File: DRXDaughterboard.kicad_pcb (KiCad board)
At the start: 8 copper layers, 150.9 x 55.8 mm, 12 parts, among them J1 Samtec_ASP-134488-01, J2 Samtec_ASP-134488-01, J3 Conn_02x12_Odd_Even, J4 Samtec_ASP-134488-01, J5 Samtec_ASP-134488-01, J6 Conn_02x06_Odd_Even, J7 Samtec_ASP-134486-01, J8 Samtec_ASP-134486-01, U1 SN74LVC2T45DCUR

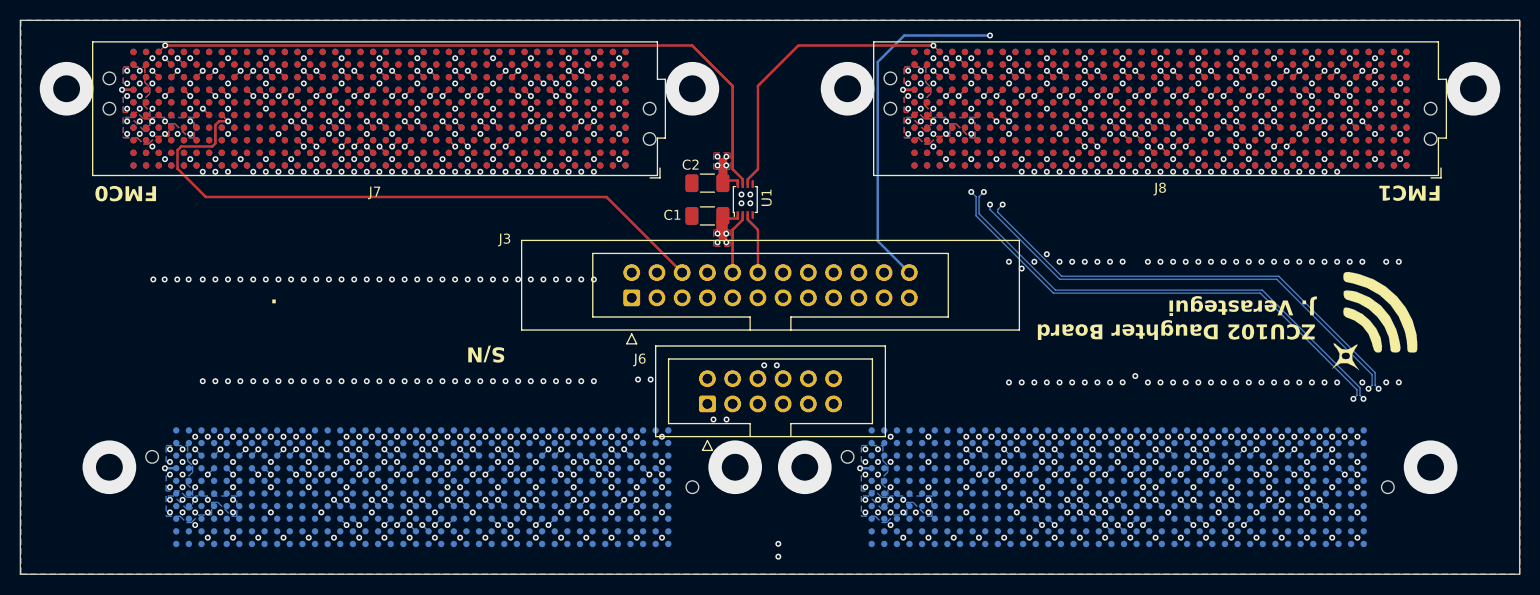
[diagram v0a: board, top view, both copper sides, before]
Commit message: Work on swapping fclk and lclk pins on J1/J4.  Add a power LED running powered by the +3.3V.  Rename.
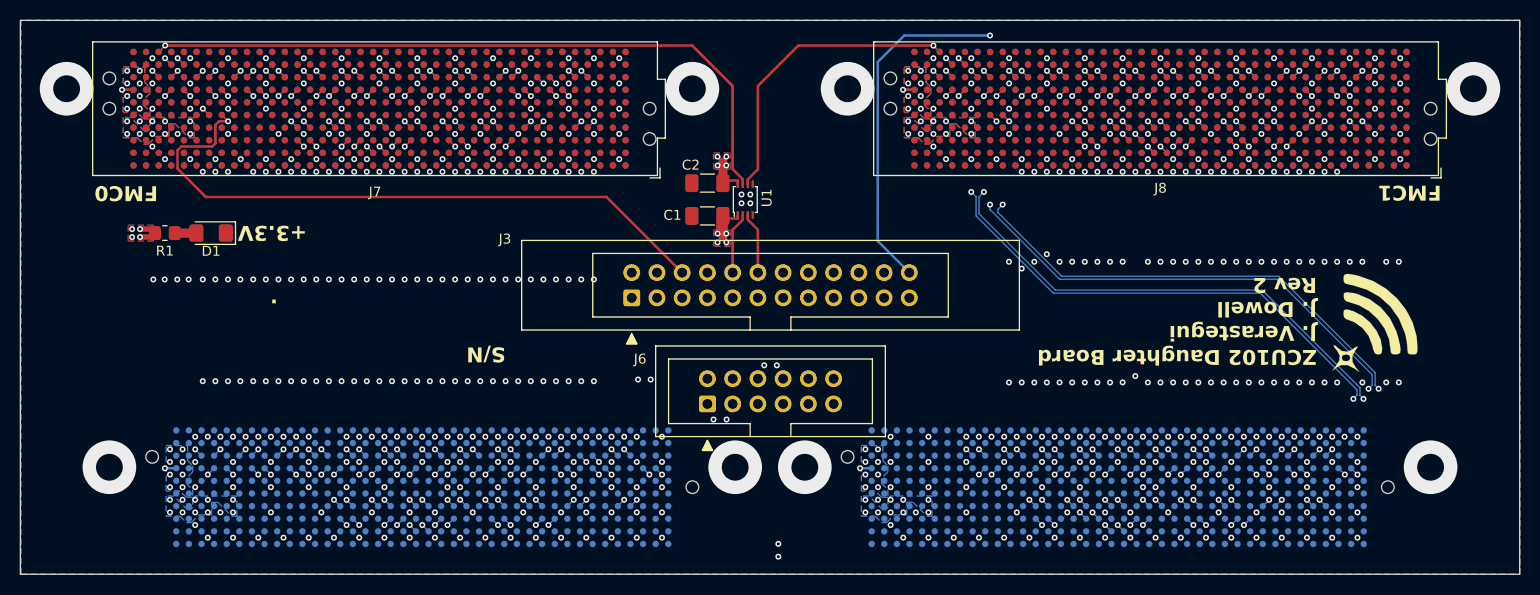
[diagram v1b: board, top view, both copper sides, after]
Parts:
- added D1: LED, LED_SMD:LED_1206_3216Metric_Pad1.42x1.75mm_HandSolder, F.Cu at (86.0, 91.6)
- added R1: 324, Resistor_SMD:R_0805_2012Metric_Pad1.20x1.40mm_HandSolder, F.Cu at (81.3, 91.6)
- moved G*** 0.19 mm to (203.7, 100.1)
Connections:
- J1 pad D4: FMC0_FCLKA_P -> FMC0_LCLKA_P
- J1 pad D5: FMC0_FCLKA_N -> FMC0_LCLKA_N
- J1 pad G2: FMC1_LCLKA_P -> FMC1_FCLKA_P
- J1 pad G3: FMC1_LCLKA_N -> FMC1_FCLKA_N
- J1 pad H4: FMC0_LCLKA_P -> FMC0_FCLKA_P
- J1 pad H5: FMC0_LCLKA_N -> FMC0_FCLKA_N
- J4 pad D4: FMC1_FCLKA_P -> FMC1_LCLKA_P
- J4 pad D5: FMC1_FCLKA_N -> FMC1_LCLKA_N
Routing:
- net FMC1_FCLKA_N: track 46.5 -> 126.5 mm
- net FMC1_FCLKA_P: track 46.5 -> 126.4 mm
- net FMC1_LCLKA_P: track 127.5 -> 50.5 mm
- net FMC1_LCLKA_N: track 127.5 -> 50.6 mm
- net FMC0_LCLKA_N: track 46.5 -> 52.1 mm
- net FMC0_FCLKA_N: track 46.5 -> 40.9 mm
- net FMC0_LCLKA_P: track 46.5 -> 52.1 mm
- net FMC0_FCLKA_P: track 46.5 -> 40.9 mm
- net +3.3VP: track 8.91 -> 12.7 mm, vias 40 -> 44
- net Net-(D1-A): track 0.00 -> 2.16 mm
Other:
- board text added: "+3.3V"
- board text added: "ZCU102 Daughter Board J. Verastegui J. Dowell Rev 2"
- board text removed: "ZCU102 Daughter Board J. Verastegui"
